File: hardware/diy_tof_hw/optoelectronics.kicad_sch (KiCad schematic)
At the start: 0 parts

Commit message: [hardware] added schematics and library components for the laser driver as well as TIA circuit
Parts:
- added C21, C5: 1p, Capacitor_SMD:C_0402_1005Metric_Pad0.74x0.62mm_HandSolder, symbol Device:C
- added C22, C23, C24, C26: 100n, Capacitor_SMD:C_0402_1005Metric_Pad0.74x0.62mm_HandSolder, symbol Device:C
- added C25: 6.8u, Capacitor_Tantalum_SMD:CP_EIA-7343-43_Kemet-X_Pad2.25x2.55mm_HandSolder, symbol Device:C_Polarized
- added C27: 2.2u, Capacitor_SMD:C_0603_1608Metric_Pad1.08x0.95mm_HandSolder, symbol Device:C
- added D1: BPW34, OptoDevice:Osram_DIL2_4.3x4.65mm_P5.08mm, symbol Sensor_Optical:BPW34
- added IC21: 74LVC1G08QW5-7, 74LVC1G08QW57, symbol 74LVC1G08QW5-7:74LVC1G08QW5-7
- added IC22: LMG1025QDEETQ1, SON65P200X200X80-7N, symbol LMG1025QDEETQ1:LMG1025QDEETQ1
- added LD1: D_Laser_Photo_MType, OptoDevice:LaserDiode_TO5-D9-3, symbol Device:D_Laser_Photo_MType
- added R21: 510, Resistor_SMD:R_0402_1005Metric_Pad0.72x0.64mm_HandSolder, symbol Device:R
- added R22: 0, Resistor_SMD:R_0402_1005Metric_Pad0.72x0.64mm_HandSolder, symbol Device:R
- added R23, R24: 2, Resistor_SMD:R_0402_1005Metric_Pad0.72x0.64mm_HandSolder, symbol Device:R
- added R25: XXX, Resistor_SMD:R_4020_10251Metric, symbol Device:R
- added R26: 51k, Resistor_SMD:R_0402_1005Metric_Pad0.72x0.64mm_HandSolder, symbol Device:R
- added RV21: 100k, Potentiometer_SMD:Potentiometer_Bourns_3224W_Vertical, symbol Device:R_Potentiometer
- added RV22, RV23: 1k, Potentiometer_SMD:Potentiometer_Bourns_3224W_Vertical, symbol Device:R_Potentiometer
- added SW1: SW_Nidec_CAS-120A1, Button_Switch_SMD:Nidec_Copal_CAS-120A, symbol Switch:SW_Nidec_CAS-120A1
- added U2: OPA858xDSG, Package_SON:WSON-8-1EP_2x2mm_P0.5mm_EP0.9x1.6mm, symbol Amplifier_Operational:OPA858xDSG
- added U3: TLV3501AIDBV, Package_TO_SOT_SMD:SOT-23-6, symbol Comparator:TLV3501AIDBV
- added V1: CSD17578Q3A, DNH0008A, symbol DNH0008A:CSD17578Q3A
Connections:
- new net: IC22.5 (OUTL), R22.1, R24.1
- new net: R23.2, R24.2, V1.4
- new net: C5.1, D1.1 (K), R26.1, U2.3 (-)
- new net: C5.2, R26.2, U2.1 (FB)
- new net: IC21.4 (Y), IC22.1 (IN+)
- new net: IC22.4 (OUTH), R22.2, R23.1
- new net: LD1.1, R25.2
- new net: LD1.2, V1.5, V1.6, V1.7, V1.8
- new net: D1.2 (A), SW1.2 (B)
- new net: RV22.2, U2.4 (+)
- new net: R21.2, RV21.1
- new net: RV23.2, U3.1 (-)
- new net: U2.6, U3.3 (+)
- new net: C21.2, IC21.2 (B), R21.1
- new net 12V_LN: SW1.1 (C)
- new net 3V3: C22.1, IC21.5 (VCC)
- new net 5V: C23.1, IC22.3 (VDD), R25.1
- new net 5V_LN: C24.1, C25.1, C26.1, C27.1, RV22.1, RV23.1, SW1.3 (A), U2.7 (V+), U2.8 (~{PD}), U3.4 (V+)
- new net GND: C22.2, C23.2, IC21.3 (GND), IC22.2 (GND), IC22.7 (EP), RV21.2, RV21.3, V1.1, V1.2, V1.3
- new net GNDA: C24.2, C25.2, C26.2, C27.2, RV22.3, RV23.3, U2.5 (V-), U2.9 (V-), U3.2 (V-), U3.6 (SHDN)
- new net LD_Pulse: C21.1, IC21.1 (A)
- new net stop_opt: U3.5
- new net ~{LD_enable}: IC22.6 (IN-)
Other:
- note added: "ACHTUNG: LASER TYP TBD, LD1 + R25 ANPASSEN!"
- note added: "ACHTUNG: PHOTODIODE TBD, ANPASSEN!"
- note added: "Decoupling capacitors"
- note added: "Laser driver"
- note added: "Pulse shortener"
- note added: "Receiver"
- note added: "Tp equals ~tau -> 0.5 ... 100 ns"

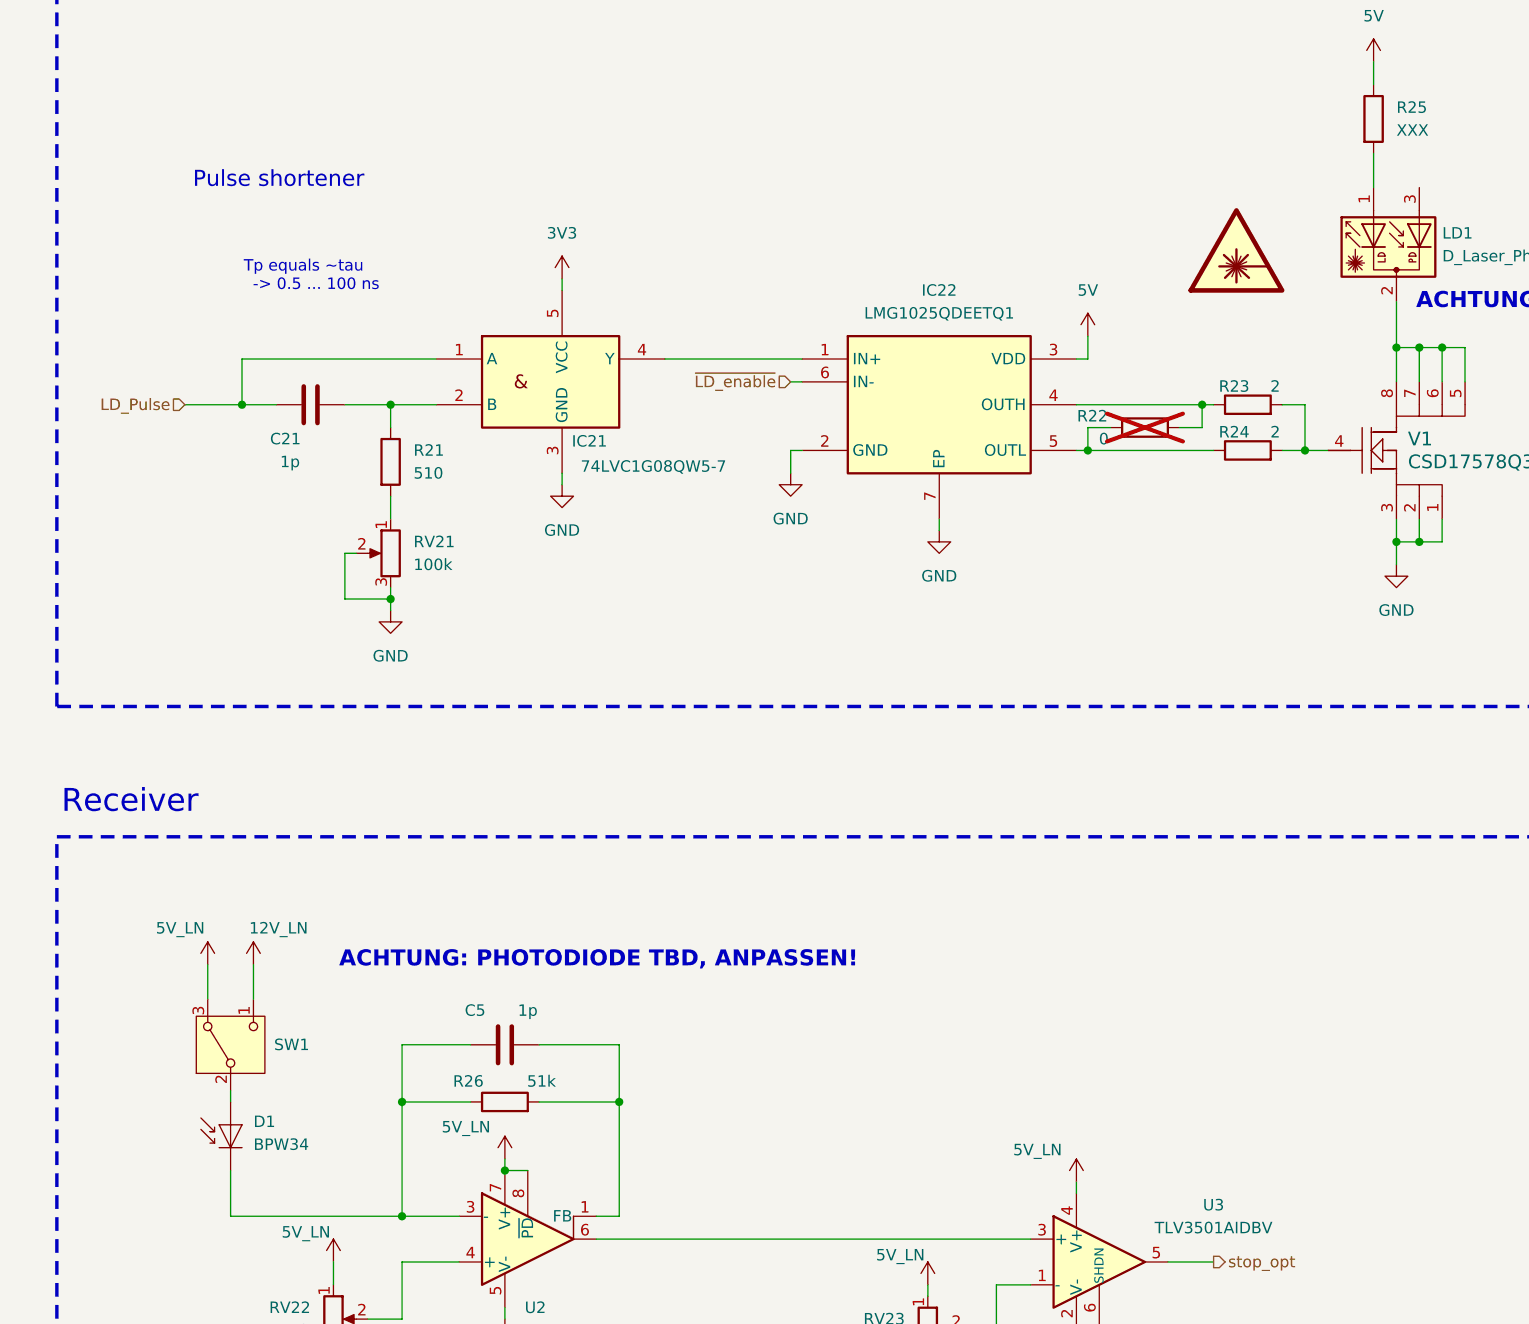
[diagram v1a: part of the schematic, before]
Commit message: [hardware] added some missing footprints. Generated a footprint for the qioptiq mount
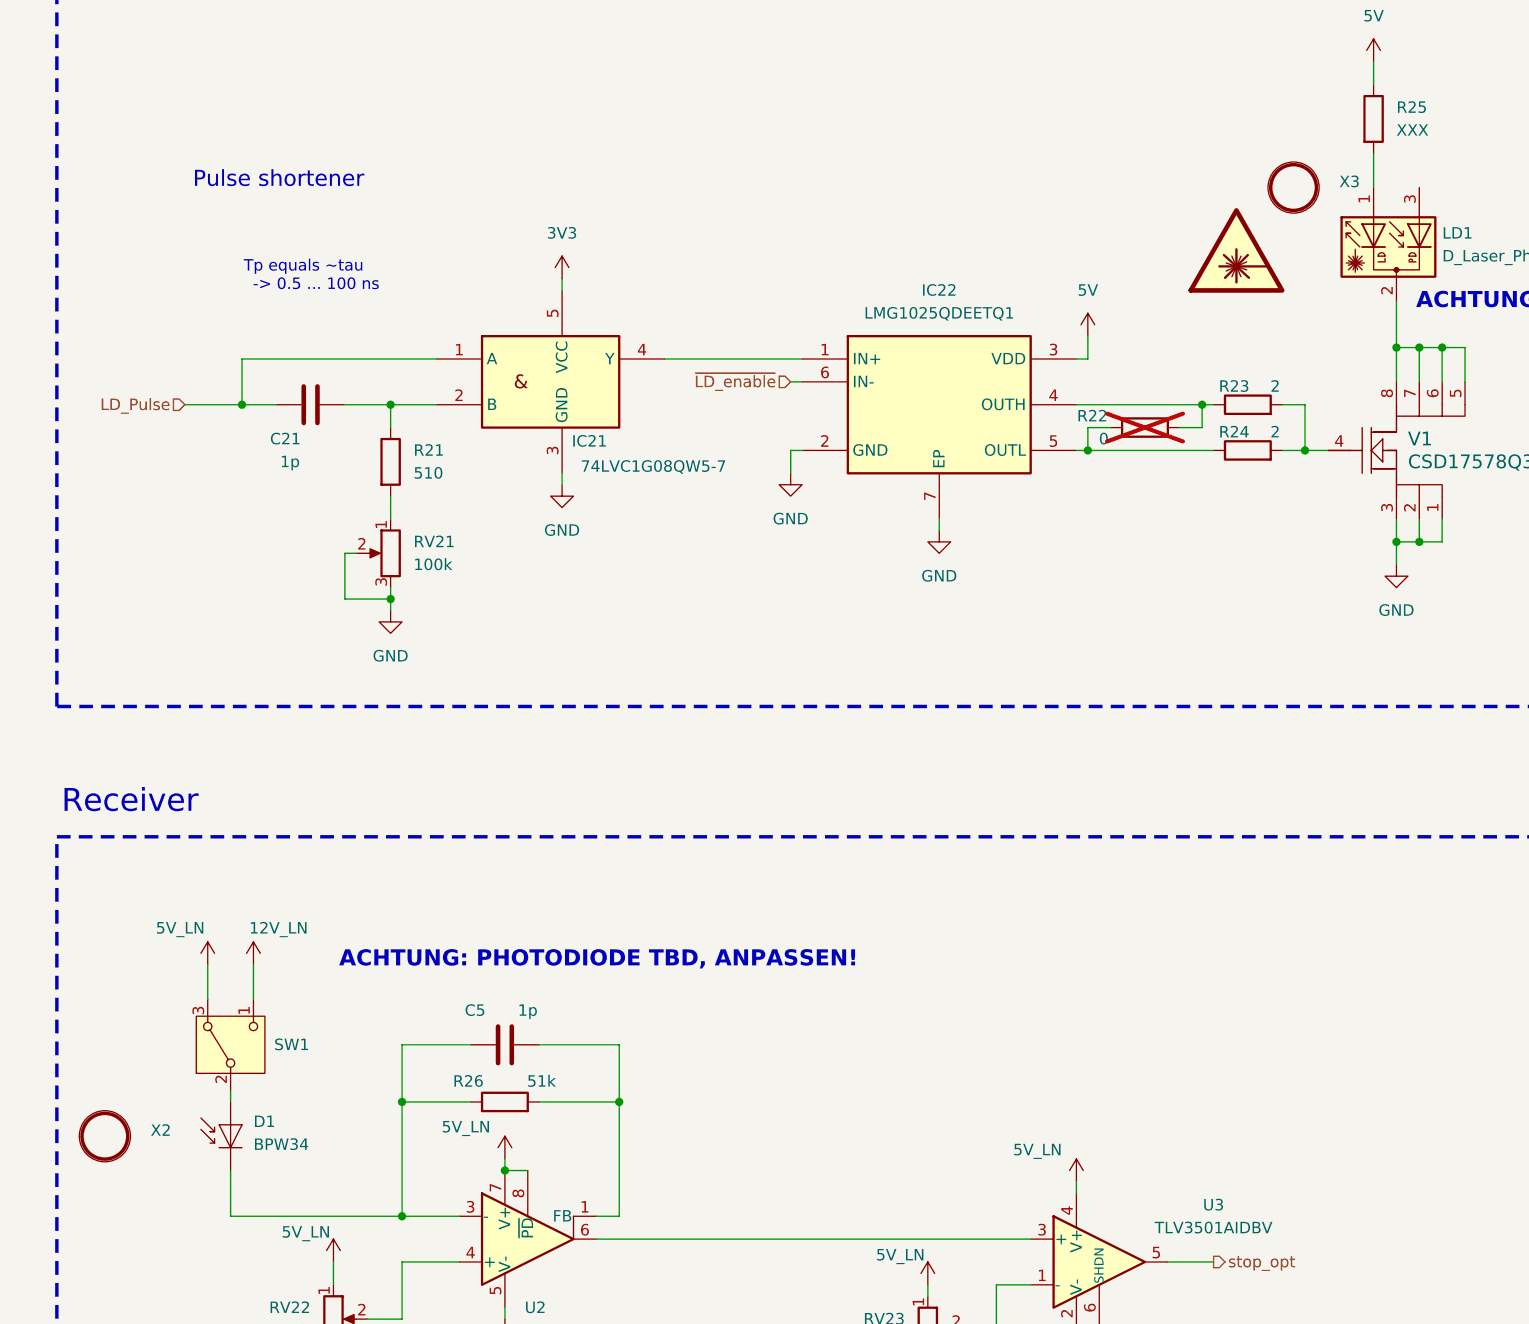
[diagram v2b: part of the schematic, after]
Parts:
- added X2, X3: ~, user:Qioptiq_Mount, symbol User_Library:Qioptiq_Mount
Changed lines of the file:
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@@
+	)
+	(symbol
+		(lib_id "User_Library:Qioptiq_Mount")
+		(at 52.07 149.86 0)
+		(unit 1)
+		(exclude_from_sim no)
+		(in_bom yes)
+		(on_board yes)
+		(dnp no)
+		(fields_autoplaced yes)
+		(property "Reference" "X2"
+			(at 57.15 149.2249 0)
+			(effects
+				(font
+					(size 1.27 1.27)
+				)
+				(justify left)
+			)
+		)
+		(property "Value" "~"
+			(at 57.15 151.13 0)
+			(effects
+				(font
+					(size 1.27 1.27)
+				)
+				(justify left)
+			)
+		)
+		(property "Footprint" "user:Qioptiq_Mount"
+			(at 52.07 149.86 0)
+			(effects
+				(font
+					(size 1.27 1.27)
+				)
+				(hide yes)
+			)
+		)
+		(property "Datasheet" ""
+			(at 52.07 149.86 0)
+			(effects
+				(font
+					(size 1.27 1.27)
+				)
+				(hide yes)
+			)
+		)
+		(property "Description" ""
+			(at 52.07 149.86 0)
+			(effects
+				(font
+					(size 1.27 1.27)
+				)
+				(hide yes)
+			)
+		)
+		(instances
+			(project ""
+				(path "/0f7bf370-0a80-4101-a61d-d850fd66ab1d/1536e9f2-3315-42ae-af66-5ae730c43aea"
+					(reference "X2")
+					(unit 1)
+				)
+			)
+		)
 	)
 	(symbol
@@
 	)
 	(symbol
+		(lib_name "Qioptiq_Mount_1")
+		(lib_id "User_Library:Qioptiq_Mount")
+		(at 184.15 44.45 0)
+		(unit 1)
+		(exclude_from_sim no)
+		(in_bom yes)
+		(on_board yes)
+		(dnp no)
+		(fields_autoplaced yes)
+		(property "Reference" "X3"
+			(at 189.23 43.8149 0)
+			(effects
+				(font
+					(size 1.27 1.27)
+				)
+				(justify left)
+			)
+		)
+		(property "Value" "~"
+			(at 189.23 45.72 0)
+			(effects
+				(font
+					(size 1.27 1.27)
+				)
+				(justify left)
+			)
+		)
+		(property "Footprint" "user:Qioptiq_Mount"
+			(at 184.15 44.45 0)
+			(effects
+				(font
+					(size 1.27 1.27)
+				)
+				(hide yes)
+			)
+		)
+		(property "Datasheet" ""
+			(at 184.15 44.45 0)
+			(effects
+				(font
+					(size 1.27 1.27)
+				)
+				(hide yes)
+			)
+		)
+		(property "Description" ""
+			(at 184.15 44.45 0)
+			(effects
+				(font
+					(size 1.27 1.27)
+				)
+				(hide yes)
+			)
+		)
+		(instances
+			(project ""
+				(path "/0f7bf370-0a80-4101-a61d-d850fd66ab1d/1536e9f2-3315-42ae-af66-5ae730c43aea"
+					(reference "X3")
+					(unit 1)
+				)
+			)
+		)
+	)
+	(symbol
 		(lib_id "DNH0008A:CSD17578Q3A")
 		(at 191.77 73.66 0)
@@
 		(at 177.8 50.8 0)
 		(unit 1)
-		(exclude_from_sim no)
+		(exclude_from_sim yes)
 		(in_bom no)
 		(on_board no)
@@
 			(at 177.8 50.8 0)
 			(effects
-				(font
-					(size 1.27 1.27)
-				)
-				(hide yes)
-			)
-		)
-		(property "Sim.Enable" "0"
-			(at 177.8 50.8 0)
-			(effects
